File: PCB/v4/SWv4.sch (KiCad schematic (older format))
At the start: 60 parts

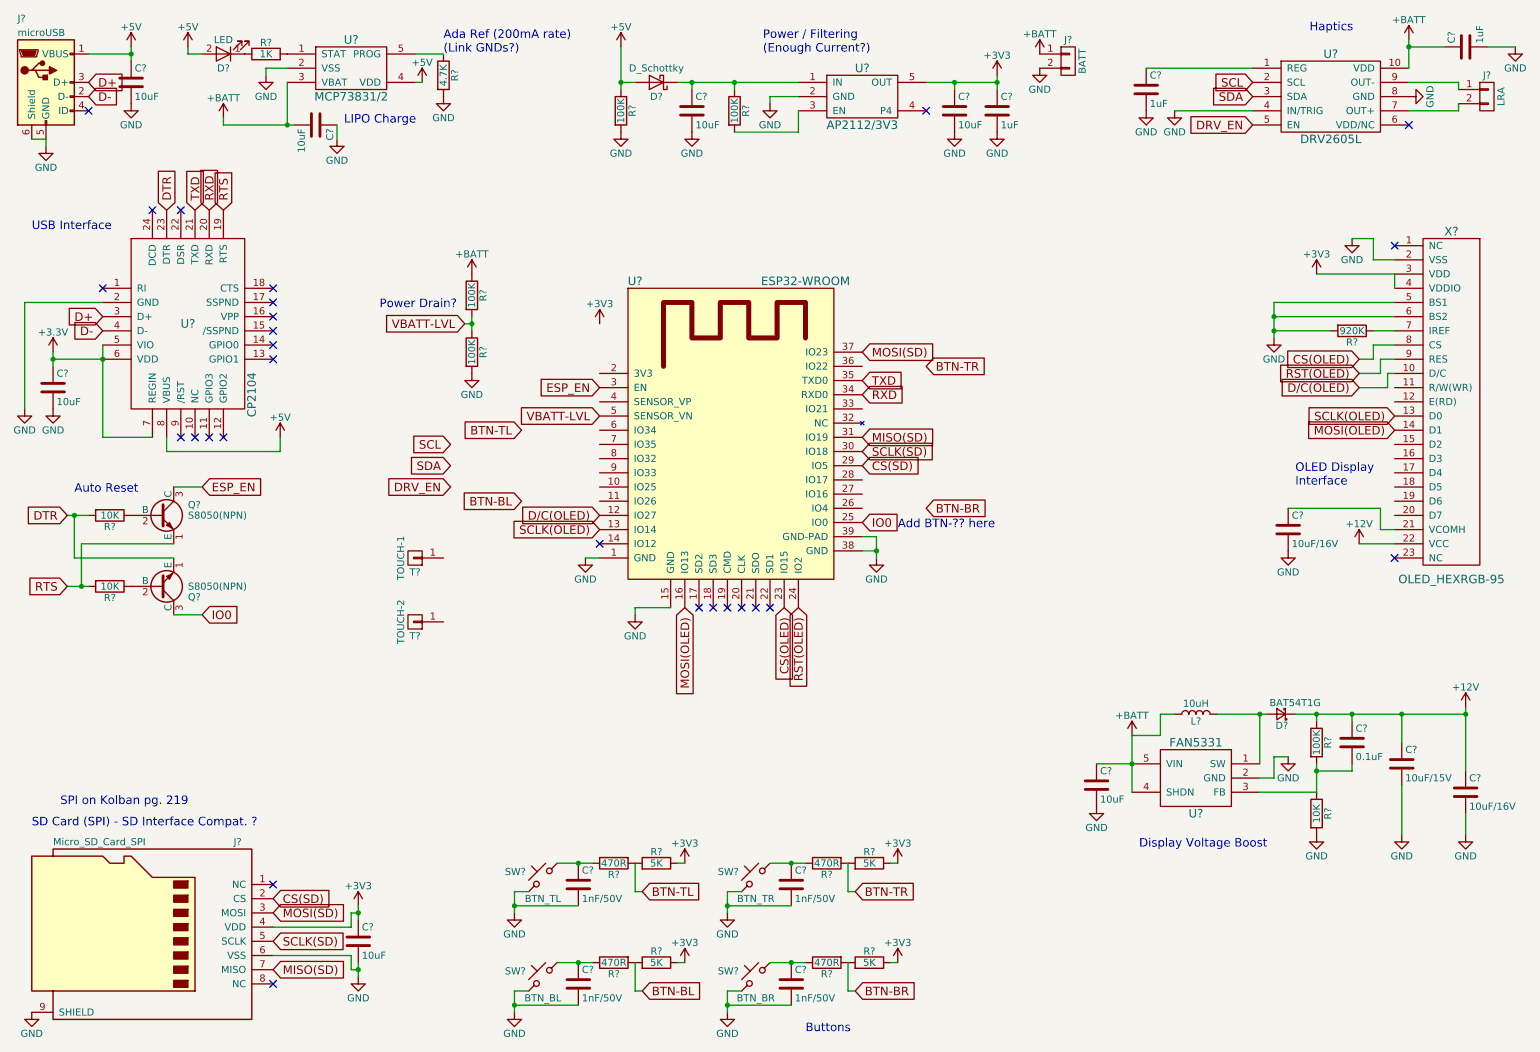
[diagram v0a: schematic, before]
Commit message: sync schem, add 9dof
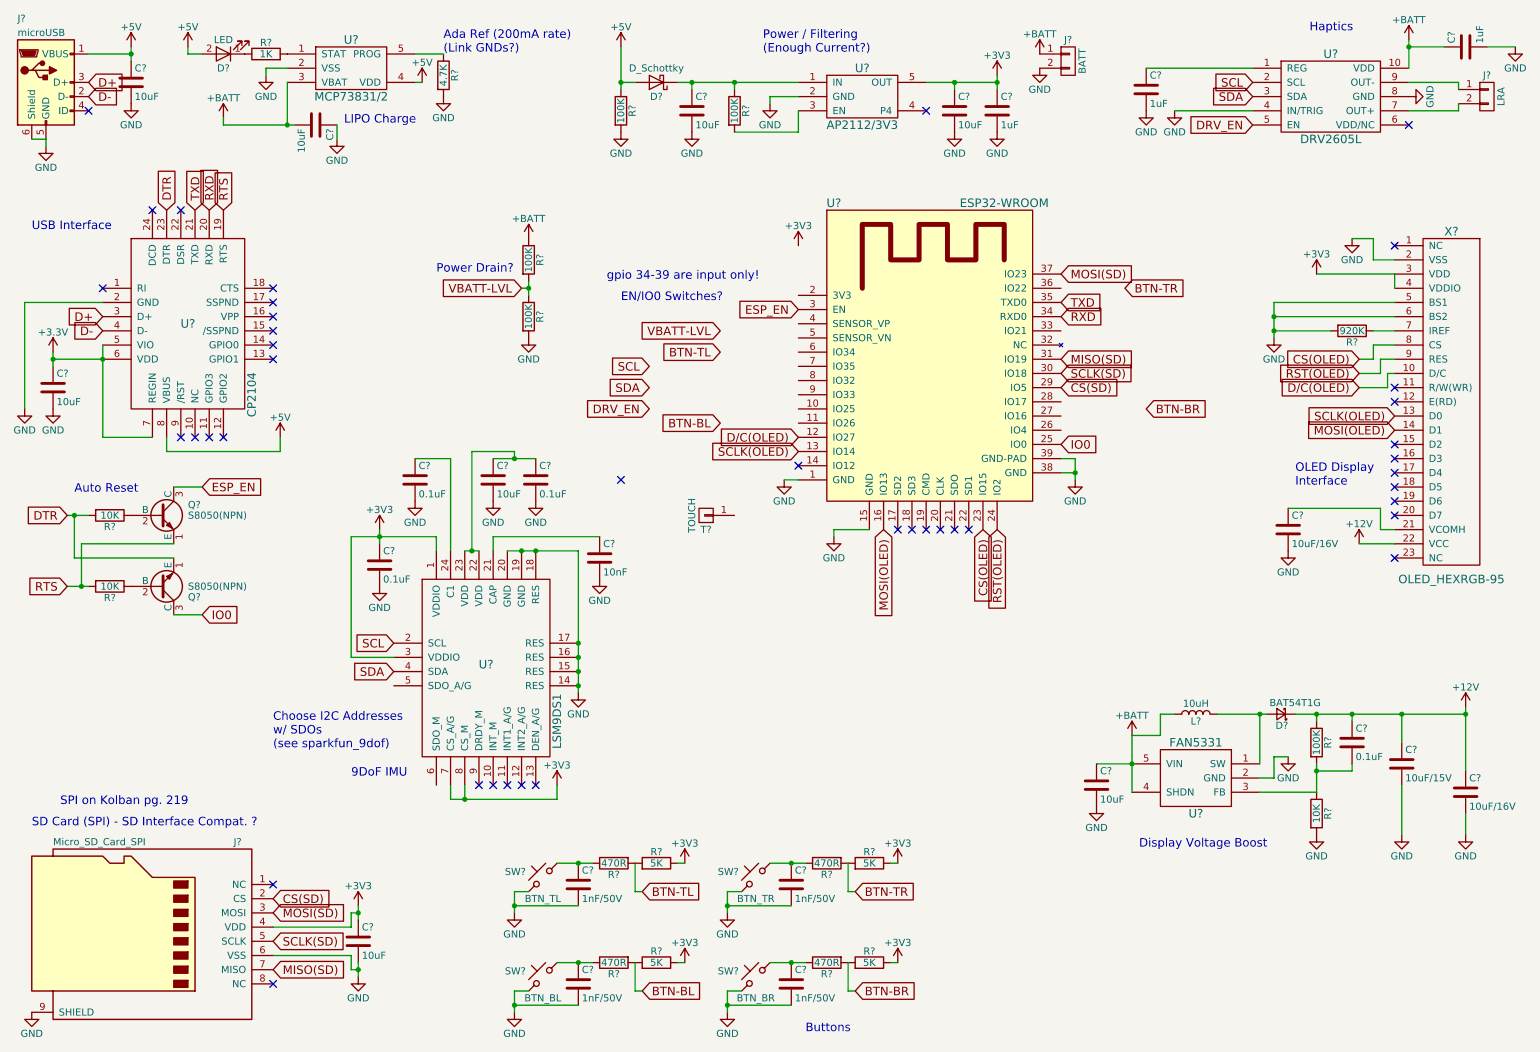
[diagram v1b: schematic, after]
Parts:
- removed T?: TOUCH-2, symbol CONN_01X01
- added C?: 10uF, symbol C
- added C? (x3): 0.1uF, symbol C
- added C?: 10nF, symbol C
- added U?: LSM9DS1, symbol LSM9DS1
- T?: value TOUCH-1 -> TOUCH
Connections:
- net +3V3: now also C?.1, U?.1 (VDDIO), U?.3 (VDDIO), U?.7 (CS_A/G), U?.8 (CS_M)
- net GND: now also C?.2, C?.2, C?.2, C?.2, C?.2, U?.14 (RES), U?.15 (RES), U?.16 (RES), U?.17 (RES), U?.18 (RES), U?.19 (GND), U?.20 (GND)
- net SCL: now also U?.2 (SCL)
- net SDA: now also U?.4 (SDA)
- net VBATT-LVL: no longer U?.5 (SENSOR_VN)
- new net: C?.1, U?.21 (CAP)
- new net: C?.1, C?.1, U?.22 (VDD), U?.23 (VDD)
- new net: C?.1, U?.24 (C1)
- no-connect marks 27 -> 41
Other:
- note added: "9DoF IMU"
- note added: "Choose I2C Addresses\nw/ SDOs\n(see sparkfun_9dof)"
- note added: "EN/IO0 Switches?"
- note added: "gpio 34-39 are input only!"
- note removed: "Add BTN-?? here"
- moved on the sheet: R?, T?, U?

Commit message: sync schem
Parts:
- added C?: 10uF, symbol C
- R?: value 5K -> 10K
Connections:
- net ESP_EN is gone; now on net BTN-TL: Q?.3 (C), U?.3 (EN)
- net +3V3: now also U?.2 (3V3), C?.1
- net BTN-BL: now also U?.6 (IO34)
- net GND: now also C?.2
- net VBATT-LVL: now also U?.4 (SENSOR_VP)
- net at U?.26 (IO4): now also T?.1 (P1)
- net IMU_INT: now reaches U?.5 (SENSOR_VN)
- net IMU_INT: now also U?.11 (INT1_A/G)
- no-connect marks 41 -> 39
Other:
- note added: "Crystal Oscillator\n(32.768 kHz)?\n[Pin 32 & 33]"
- note added: "gpio 34-39\ninput only!"
- note removed: "EN/IO0 Switches?"
- note removed: "gpio 34-39 are input only!"
- moved on the sheet: J?, R?, T?
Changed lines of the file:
@@
 Text Notes 9650 650  0    60   ~ 0
 Haptics
-Text GLabel 5500 2900 0    60   Input ~ 0
+Text GLabel 5850 2600 0    60   Input ~ 0
 BTN-TL
-Text GLabel 5500 3400 0    60   Input ~ 0
+Text GLabel 6050 2900 0    60   Input ~ 0
 BTN-BL
-Text GLabel 8350 2450 2    60   Input ~ 0
+Text GLabel 8500 2450 2    60   Input ~ 0
 BTN-TR
 Text GLabel 8500 3300 2    60   Input ~ 0
@@
 Text GLabel 6050 3500 0    60   Input ~ 0
 D/C(OLED)
-Text GLabel 5000 3000 0    60   Input ~ 0
+Text GLabel 5050 3200 0    60   Input ~ 0
 SCL
-Text GLabel 5000 3150 0    60   Input ~ 0
+Text GLabel 5050 3350 0    60   Input ~ 0
 SDA
 Text GLabel 1800 1900 1    60   Input ~ 0
@@
 L +3V3 #PWR?
 U 1 1 5904C3E7
-P 6050 2150
-F 0 "#PWR?" H 6050 2000 50  0001 C CNN
-F 1 "+3V3" H 6050 2290 50  0000 C CNN
-F 2 "" H 6050 2150 50  0001 C CNN
-F 3 "" H 6050 2150 50  0001 C CNN
-	1    6050 2150
+P 6050 2500
+F 0 "#PWR?" H 6050 2350 50  0001 C CNN
+F 1 "+3V3" H 6050 2640 50  0000 C CNN
+F 2 "" H 6050 2500 50  0001 C CNN
+F 3 "" H 6050 2500 50  0001 C CNN
+	1    6050 2500
 	1    0    0    -1
 $EndComp
@@
 Text GLabel 1850 3850 2    60   Input ~ 0
 ESP_EN
-Text GLabel 6050 2600 0    60   Input ~ 0
+Text GLabel 5850 2500 0    60   Input ~ 0
 ESP_EN
 Text GLabel 1850 4750 2    60   Input ~ 0
@@
 P 5050 6500
 F 0 "R?" V 5130 6500 50  0000 C CNN
-F 1 "5K" V 5050 6500 50  0000 C CNN
+F 1 "10K" V 5050 6500 50  0000 C CNN
 F 2 "" V 4980 6500 50  0001 C CNN
 F 3 "" H 5050 6500 50  0001 C CNN
@@
 L CONN_01X02 J?
 U 1 1 59247EF5
-P 7950 850
-F 0 "J?" H 7950 1000 50  0000 C CNN
-F 1 "BATT" V 8050 850 50  0000 C CNN
-F 2 "" H 7950 850 50  0001 C CNN
-F 3 "" H 7950 850 50  0001 C CNN
-	1    7950 850
+P 7850 750
+F 0 "J?" H 7850 900 50  0000 C CNN
+F 1 "BATT" V 7950 750 50  0000 C CNN
+F 2 "" H 7850 750 50  0001 C CNN
+F 3 "" H 7850 750 50  0001 C CNN
+	1    7850 750
 	1    0    0    -1
 $EndComp
@@
 L +BATT #PWR?
 U 1 1 59248DC0
-P 7750 800
-F 0 "#PWR?" H 7750 650 50  0001 C CNN
-F 1 "+BATT" H 7750 940 50  0000 C CNN
-F 2 "" H 7750 800 50  0001 C CNN
-F 3 "" H 7750 800 50  0001 C CNN
-	1    7750 800
+P 7650 700
+F 0 "#PWR?" H 7650 550 50  0001 C CNN
+F 1 "+BATT" H 7650 840 50  0000 C CNN
+F 2 "" H 7650 700 50  0001 C CNN
+F 3 "" H 7650 700 50  0001 C CNN
+	1    7650 700
 	1    0    0    -1
 $EndComp
@@
 L GND #PWR?
 U 1 1 592491EE
-P 7750 900
-F 0 "#PWR?" H 7750 650 50  0001 C CNN
-F 1 "GND" H 7750 750 50  0000 C CNN
-F 2 "" H 7750 900 50  0001 C CNN
-F 3 "" H 7750 900 50  0001 C CNN
-	1    7750 900
+P 7650 800
+F 0 "#PWR?" H 7650 550 50  0001 C CNN
+F 1 "GND" H 7650 650 50  0000 C CNN
+F 2 "" H 7650 800 50  0001 C CNN
+F 3 "" H 7650 800 50  0001 C CNN
+	1    7650 800
 	1    0    0    -1
 $EndComp
@@
 L R R?
 U 1 1 5924E8FD
-P 4150 2250
-F 0 "R?" V 4230 2250 50  0000 C CNN
-F 1 "100K" V 4150 2250 50  0000 C CNN
-F 2 "" V 4080 2250 50  0001 C CNN
-F 3 "" H 4150 2250 50  0001 C CNN
-	1    4150 2250
+P 3150 2050
+F 0 "R?" V 3230 2050 50  0000 C CNN
+F 1 "100K" V 3150 2050 50  0000 C CNN
+F 2 "" V 3080 2050 50  0001 C CNN
+F 3 "" H 3150 2050 50  0001 C CNN
+	1    3150 2050
 	1    0    0    -1
 $EndComp
@@
 L R R?
 U 1 1 5924EA32
-P 4150 2650
-F 0 "R?" V 4230 2650 50  0000 C CNN
-F 1 "100K" V 4150 2650 50  0000 C CNN
-F 2 "" V 4080 2650 50  0001 C CNN
-F 3 "" H 4150 2650 50  0001 C CNN
-	1    4150 2650
+P 3150 2450
+F 0 "R?" V 3230 2450 50  0000 C CNN
+F 1 "100K" V 3150 2450 50  0000 C CNN
+F 2 "" V 3080 2450 50  0001 C CNN
+F 3 "" H 3150 2450 50  0001 C CNN
+	1    3150 2450
 	1    0    0    -1
 $EndComp
@@
 L GND #PWR?
 U 1 1 5924EADE
-P 4150 2800
-F 0 "#PWR?" H 4150 2550 50  0001 C CNN
-F 1 "GND" H 4150 2650 50  0000 C CNN
-F 2 "" H 4150 2800 50  0001 C CNN
-F 3 "" H 4150 2800 50  0001 C CNN
-	1    4150 2800
+P 3150 2600
+F 0 "#PWR?" H 3150 2350 50  0001 C CNN
+F 1 "GND" H 3150 2450 50  0000 C CNN
+F 2 "" H 3150 2600 50  0001 C CNN
+F 3 "" H 3150 2600 50  0001 C CNN
+	1    3150 2600
 	1    0    0    -1
 $EndComp
@@
 L +BATT #PWR?
 U 1 1 5924EB66
-P 4150 2100
-F 0 "#PWR?" H 4150 1950 50  0001 C CNN
-F 1 "+BATT" H 4150 2240 50  0000 C CNN
-F 2 "" H 4150 2100 50  0001 C CNN
-F 3 "" H 4150 2100 50  0001 C CNN
-	1    4150 2100
-	1    0    0    -1
-$EndComp
-Text GLabel 4100 2450 0    60   Input ~ 0
+P 3150 1900
+F 0 "#PWR?" H 3150 1750 50  0001 C CNN
+F 1 "+BATT" H 3150 2040 50  0000 C CNN
+F 2 "" H 3150 1900 50  0001 C CNN
+F 3 "" H 3150 1900 50  0001 C CNN
+	1    3150 1900
+	1    0    0    -1
+$EndComp
+Text GLabel 3100 2250 0    60   Input ~ 0
 VBATT-LVL
-Text GLabel 5500 2750 0    60   Input ~ 0
+Text GLabel 6050 2700 0    60   Input ~ 0
 VBATT-LVL
 Text GLabel 7900 2350 2    60   Input ~ 0
@@
 NoConn ~ 7150 4150
 NoConn ~ 7250 4150
-Text Notes 3500 2350 0    60   ~ 0
+Text Notes 2500 2150 0    60   ~ 0
 Power Drain?
-Text GLabel 5000 3300 0    60   Input ~ 0
+Text GLabel 5050 3500 0    60   Input ~ 0
 DRV_EN
 Text GLabel 7900 2950 2    60   Input ~ 0
@@
 L CONN_01X01 T?
 U 1 1 593078C7
-P 5400 4050
-F 0 "T?" H 5400 4150 50  0000 C CNN
-F 1 "TOUCH" V 5500 4050 50  0000 C CNN
-F 2 "" H 5400 4050 50  0001 C CNN
-F 3 "" H 5400 4050 50  0001 C CNN
-	1    5400 4050
-	-1   0    0    1
+P 8250 3650
+F 0 "T?" H 8250 3750 50  0000 C CNN
+F 1 "TOUCH" V 8350 3650 50  0000 C CNN
+F 2 "" H 8250 3650 50  0001 C CNN
+F 3 "" H 8250 3650 50  0001 C CNN
+	1    8250 3650
+	0    1    1    0
 $EndComp
 $Comp
@@
 L +3V3 #PWR?
 U 1 1 5931D032
-P 4350 5950
-F 0 "#PWR?" H 4350 5800 50  0001 C CNN
-F 1 "+3V3" H 4350 6090 50  0000 C CNN
-F 2 "" H 4350 5950 50  0001 C CNN
-F 3 "" H 4350 5950 50  0001 C CNN
-	1    4350 5950
+P 3800 6250
+F 0 "#PWR?" H 3800 6100 50  0001 C CNN
+F 1 "+3V3" H 3800 6390 50  0000 C CNN
+F 2 "" H 3800 6250 50  0001 C CNN
+F 3 "" H 3800 6250 50  0001 C CNN
+	1    3800 6250
 	1    0    0    -1
 $EndComp
 Text Notes 2350 5700 0    60   ~ 0
 Choose I2C Addresses\nw/ SDOs\n(see sparkfun_9dof)
-Text Notes 4800 2550 0    60   ~ 0
-EN/IO0 Switches?
 NoConn ~ 3800 5950
 NoConn ~ 3900 5950
-NoConn ~ 4000 5950
 NoConn ~ 4100 5950
 NoConn ~ 4200 5950
@@
 NoConn ~ 10250 3950
 NoConn ~ 10250 4050
-NoConn ~ 4800 3800
+Text Notes 4900 2900 0    60   ~ 0
+gpio 34-39\ninput only!
+Text GLabel 4000 5950 3    60   Input ~ 0
+IMU_INT
+Text GLabel 6050 2800 0    60   Input ~ 0
+IMU_INT
+$Comp
+L +3V3 #PWR?
+U 1 1 5932A15F
+P 7900 1050
+F 0 "#PWR?" H 7900 900 50  0001 C CNN
+F 1 "+3V3" H 7900 1190 50  0000 C CNN
+F 2 "" H 7900 1050 50  0001 C CNN
+F 3 "" H 7900 1050 50  0001 C CNN
+	1    7900 1050
+	1    0    0    -1
+$EndComp
+$Comp
+L GND #PWR?
+U 1 1 5932A1F5
+P 7900 1350
+F 0 "#PWR?" H 7900 1100 50  0001 C CNN
+F 1 "GND" H 7900 1200 50  0000 C CNN
+F 2 "" H 7900 1350 50  0001 C CNN
+F 3 "" H 7900 1350 50  0001 C CNN
+	1    7900 1350
+	1    0    0    -1
+$EndComp
+$Comp
+L C C?
+U 1 1 5932A28B
+P 7900 1200
+F 0 "C?" H 7925 1300 50  0000 L CNN
+F 1 "10uF" H 7925 1100 50  0000 L CNN
+F 2 "" H 7938 1050 50  0001 C CNN
+F 3 "" H 7900 1200 50  0001 C CNN
+	1    7900 1200
+	1    0    0    -1
+$EndComp
 Wire Wire Line
 	10350 1000 10700 1000
@@
 Connection ~ 4800 1000
 Wire Wire Line
-	4150 2400 4150 2450
-Wire Wire Line
-	4150 2450 4150 2500
-Connection ~ 4150 2450
-Wire Wire Line
-	4100 2450 4150 2450
+	3150 2200 3150 2250
+Wire Wire Line
+	3150 2250 3150 2300
+Connection ~ 3150 2250
+Wire Wire Line
+	3100 2250 3150 2250
 Wire Wire Line
 	2900 6950 2900 6850
@@
 	3600 6050 3600 5950
 Wire Wire Line
-	3700 6050 3700 5950
+	3700 5950 3700 6050
+Wire Wire Line
+	3700 6050 3700 6300
 Wire Wire Line
 	3600 6050 3700 6050
-Wire Wire Line
-	3700 6050 4350 6050
-Wire Wire Line
-	4350 6050 4350 5950
 Connection ~ 3700 6050
-Text Notes 4700 2400 0    60   ~ 0
-gpio 34-39 are input only!
+Wire Wire Line
+	3700 6300 3800 6300
+Wire Wire Line
+	3800 6300 3800 6250
+Wire Wire Line
+	7900 3450 8250 3450
+Wire Wire Line
+	5850 2500 5950 2500
+Wire Wire Line
+	5950 2500 5950 2600
+Wire Wire Line
+	5850 2600 5950 2600
+Wire Wire Line
+	5950 2600 6050 2600
+Connection ~ 5950 2600
+Text Notes 4000 3100 0    60   ~ 0
+Crystal Oscillator\n(32.768 kHz)?\n[Pin 32 & 33]
 $EndSCHEMATC
